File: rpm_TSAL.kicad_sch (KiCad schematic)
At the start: 2 parts, among them J1 Conn_01x02, J5 Conn_01x02

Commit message: Misc.
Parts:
- added J16, J17, J18, J19, J20: Conn_01x01, symbol Connector_Generic:Conn_01x01
- added J21, J22: Conn_01x02, symbol Connector_Generic:Conn_01x02

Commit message: TSAL Rev 0.2
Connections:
- net  HV+ renamed HV+
- net  HV_RED+ renamed HV_RED+
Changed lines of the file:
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@@
 		(title "TSAL")
 		(date "2024-07-11")
-		(rev "V0.1")
+		(rev "V0.2")
 		(company "Team RPM - UAS Münster")
 		(comment 1 "Luca Sapion")
@@
 			)
 		)
-		(property "Value" " HV+"
+		(property "Value" "HV+"
 			(at 140.97 163.83 0)
 			(effects
@@
 			)
 		)
-		(property "Value" " HV_RED+"
+		(property "Value" "HV_RED+"
 			(at 53.34 85.09 0)
 			(effects
@@
 			)
 		)
-		(property "Value" " HV_RED+"
+		(property "Value" "HV_RED+"
 			(at 73.66 163.83 0)
 			(effects
@@
 			)
 		)
-		(property "Value" " HV+"
+		(property "Value" "HV+"
 			(at 97.79 85.09 0)
 			(effects

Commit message: Added Seperate Project
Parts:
- removed J16, J17: Conn_01x01, symbol Connector_Generic:Conn_01x01
- removed J22: Conn_01x02, symbol Connector_Generic:Conn_01x02
- removed J5: Conn_01x02, wuerth_conn:657002130101, symbol Connector_Generic:Conn_01x02
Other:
- note removed: "TS Sense RED Connector"
- moved on the sheet: J1, J18, J19, J20, J21

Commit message: Added Sub project
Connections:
- net HV+: now also J1.2 (Pin_2); no longer J1.1 (Pin_1)
- net HV-: now also J1.1 (Pin_1); no longer J1.2 (Pin_2)
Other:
- removed sheet TSAL RED
- sheet LV Connectors ports: added none; removed TSAL_LED_RED

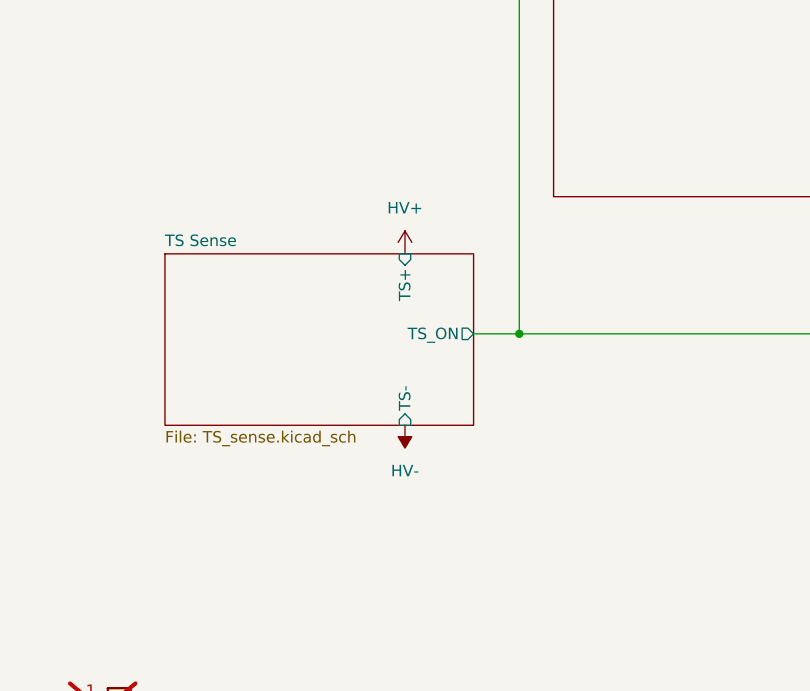
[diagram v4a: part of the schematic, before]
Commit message: Added TSAC Indicator with PSU
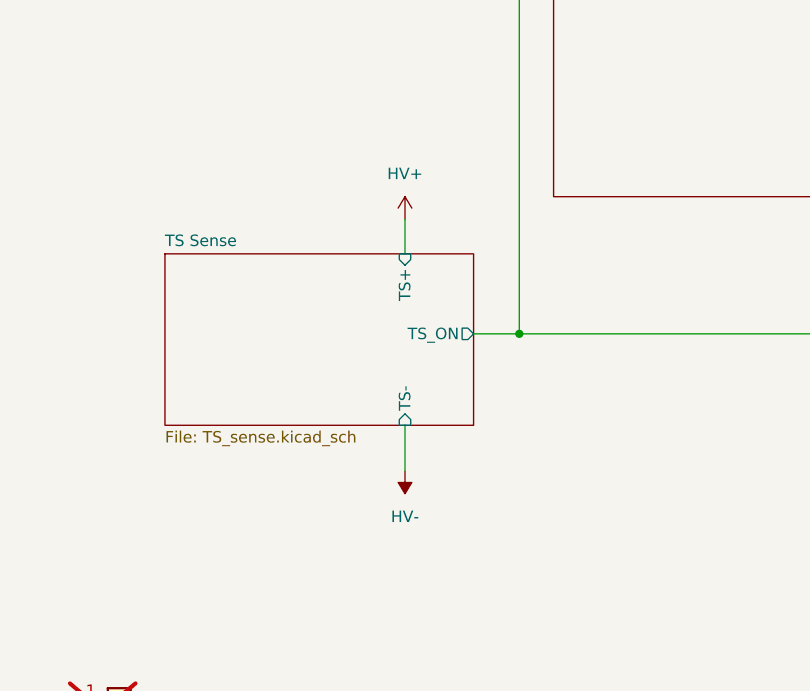
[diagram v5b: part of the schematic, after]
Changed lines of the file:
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@@
+	(wire
+		(pts
+			(xy 97.79 109.22) (xy 97.79 114.3)
+		)
+		(stroke
+			(width 0)
+			(type default)
+		)
+	)
 	(wire
 		(pts
@@
 		(pts
 			(xy 193.04 71.12) (xy 203.2 71.12)
+		)
+		(stroke
+			(width 0)
+			(type default)
+		)
+	)
+	(wire
+		(pts
+			(xy 97.79 86.36) (xy 97.79 90.17)
 		)
 		(stroke
@@
 	(symbol
 		(lib_id "power:-6V")
-		(at 97.79 109.22 180)
+		(at 97.79 114.3 180)
 		(unit 1)
 		(exclude_from_sim no)
@@
 		(fields_autoplaced yes)
 		(property "Reference" "#PWR012"
-			(at 97.79 105.41 0)
+			(at 97.79 110.49 0)
 			(effects
 				(font
@@
 		)
 		(property "Value" "HV-"
+			(at 97.79 119.38 0)
+			(effects
+				(font
+					(size 1.27 1.27)
+				)
+			)
+		)
+		(property "Footprint" ""
 			(at 97.79 114.3 0)
 			(effects
@@
 					(size 1.27 1.27)
 				)
-			)
-		)
-		(property "Footprint" ""
-			(at 97.79 109.22 0)
-			(effects
-				(font
-					(size 1.27 1.27)
-				)
 				(hide yes)
 			)
 		)
 		(property "Datasheet" ""
-			(at 97.79 109.22 0)
+			(at 97.79 114.3 0)
 			(effects
 				(font
@@
 		)
 		(property "Description" "Power symbol creates a global label with name \"-6V\""
-			(at 97.79 109.22 0)
+			(at 97.79 114.3 0)
 			(effects
 				(font
@@
 	(symbol
 		(lib_id "power:+7.5V")
-		(at 97.79 90.17 0)
+		(at 97.79 86.36 0)
 		(unit 1)
 		(exclude_from_sim no)
@@
 		(fields_autoplaced yes)
 		(property "Reference" "#PWR06"
-			(at 97.79 93.98 0)
+			(at 97.79 90.17 0)
 			(effects
 				(font
@@
 		)
 		(property "Value" "HV+"
-			(at 97.79 85.09 0)
+			(at 97.79 81.28 0)
 			(effects
 				(font
@@
 		)
 		(property "Footprint" ""
-			(at 97.79 90.17 0)
+			(at 97.79 86.36 0)
 			(effects
 				(font
@@
 		)
 		(property "Datasheet" ""
-			(at 97.79 90.17 0)
+			(at 97.79 86.36 0)
 			(effects
 				(font
@@
 		)
 		(property "Description" "Power symbol creates a global label with name \"+7.5V\""
-			(at 97.79 90.17 0)
-			(effects
-				(font
+			(at 97.79 86.36 0)
+			(effects
+				(font
